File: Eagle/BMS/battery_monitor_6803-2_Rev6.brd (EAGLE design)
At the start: 88.1 x 53.3 mm, 68 parts, among them IC1 MIC2954-03WS, Q1 MOSFET-PCHANNELIRLML2244, Q10 IRF9530, Q2 MOSFET-NCHANNELBSS138, Q3 MOSFET-PCHANNELIRLML2244, Q4 MOSFET-PCHANNELIRLML2244, Q5 MOSFET-PCHANNELIRLML2244, Q6 MOSFET-NCHANNELBSS138, Q7 MOSFET-NCHANNELBSS138, Q8 MOSFET-NCHANNELBSS138, Q9 PMOS_AO4435

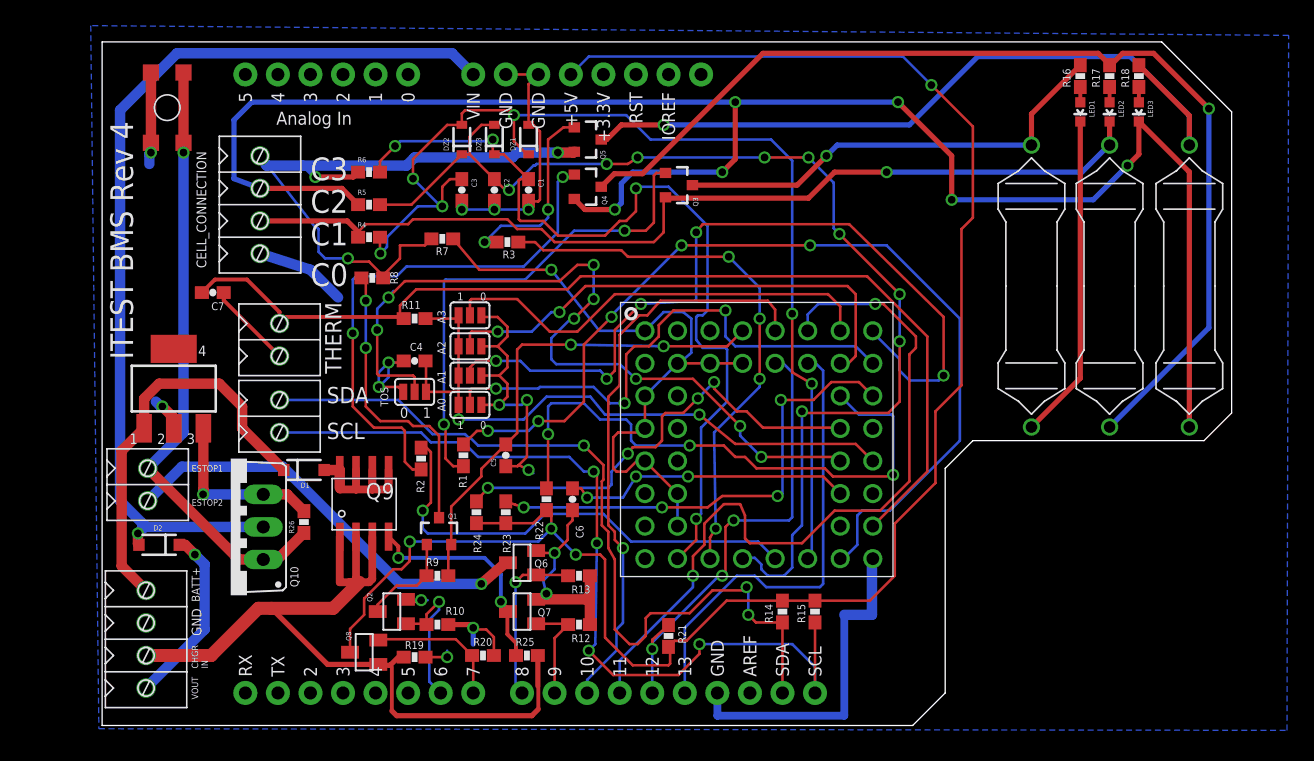
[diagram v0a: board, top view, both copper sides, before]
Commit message: Added voltage regulator to charging circuit of BMS.
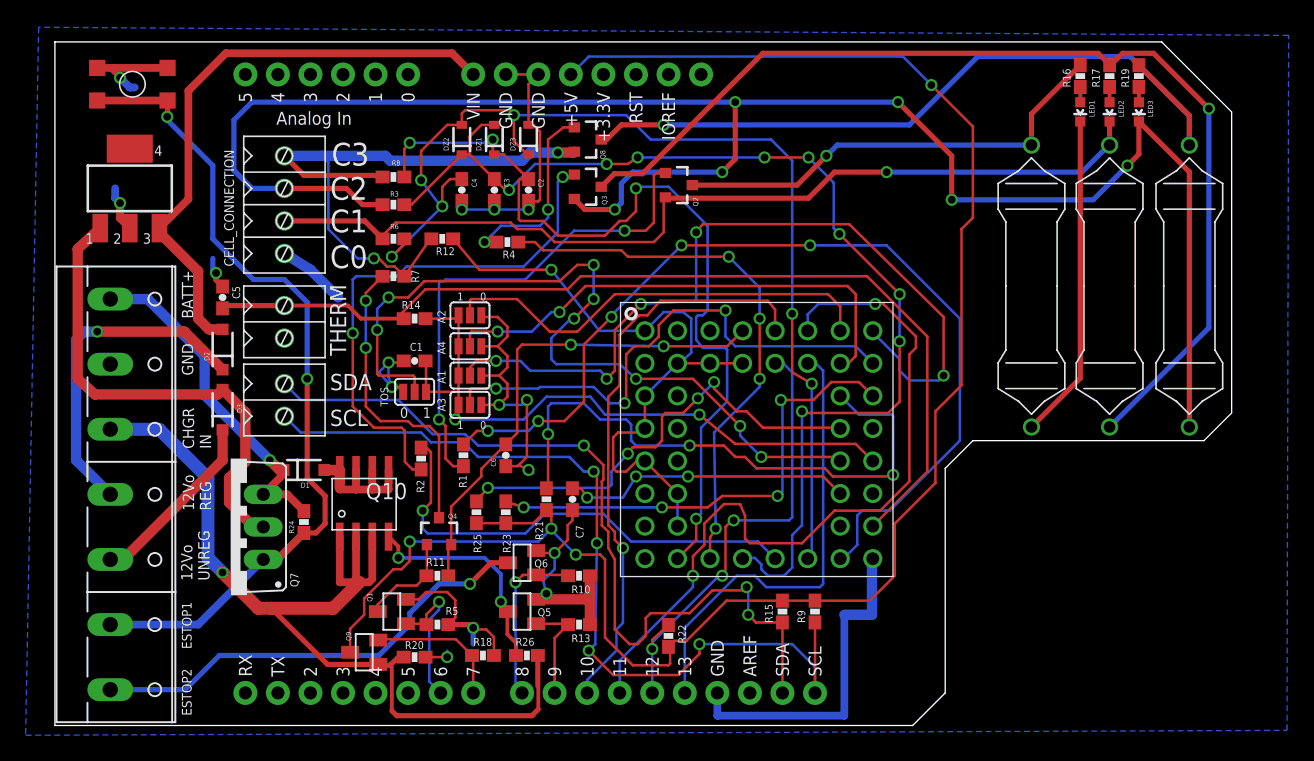
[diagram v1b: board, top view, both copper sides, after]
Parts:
- removed A0: (no value), SparkFun:SJ_3
- removed U$7: TACTILE-SWITCH-7914G, GeekAmmo:7914G
- removed U$8: ARDUINO_R3_SHIELD, SparkFun-Boards:UNO_R3_SHIELD
- removed U$9: LTC6803, Clayton:LTC6803_BREAKOUT
- added A4: (no value), SparkFun:SJ_3
- added D3: SMD26PL-TP, SparkFun-DiscreteSemi:SOD-123
- added U$5: RESISTOR-POWER-3W, isaac1:RESISTOR-3W
- added X1: W237-07P, con-wago-508:W237-7P
- C1: value 0.1uF -> 1uF
- C4: value 1uF -> 0.1uF
- Q1, Q5: value MOSFET-PCHANNELIRLML2244 -> MOSFET-NCHANNELBSS138; device SparkFun-DiscreteSemi:SOT23-3@1 -> SparkFun-DiscreteSemi:SOT23
- Q10: value IRF9530 -> PMOS_AO4435; device Adams Chips:TO220BV -> isaac1:SOIC8
- Q2, Q8: value MOSFET-NCHANNELBSS138 -> MOSFET-PCHANNELIRLML2244; device SparkFun-DiscreteSemi:SOT23 -> SparkFun-DiscreteSemi:SOT23-3@1
- Q7: value MOSFET-NCHANNELBSS138 -> IRF9530; device SparkFun-DiscreteSemi:SOT23 -> Adams Chips:TO220BV
- Q9: value PMOS_AO4435 -> MOSFET-NCHANNELBSS138; device isaac1:SOIC8 -> SparkFun-DiscreteSemi:SOT23
- R11: value 100k -> 4.7k
- R12: value 4.7k -> 100
- R14: value 4.7k -> 100k
- R18: value 470 -> 4.7k
- R19: value 4.7k -> 470
- R21, R25: value 4.7k -> 1Meg
- R22, R26: value 1Meg -> 4.7k
- R3: value 3.3k -> 100
- R4: value 100 -> 3.3k
- R5: value 100 -> 4.7k
- U$2: value RESISTOR-POWER-3W -> TACTILE-SWITCH-7914G; device isaac1:RESISTOR-3W -> GeekAmmo:7914G
- U$4: value SCREW_TERMINAL_4 -> LTC6803; device isaac1:SCREW_TERMINAL_4 -> Clayton:LTC6803_BREAKOUT
- U$6: value SCREW_TERMINAL_2 -> ARDUINO_R3_SHIELD; device Isaac:SCREW_TERMINAL_2 -> SparkFun-Boards:UNO_R3_SHIELD
- moved U$2 80.8 mm to (1.14, 52.1), turned to 270 degrees
- moved R19 72.5 mm to (82.4, 51.4), turned to 90 degrees
- moved R18 68.3 mm to (31.2, 6.22), turned to 180 degrees
- moved U$6 65.0 mm to (67.3, 0.76), turned to 90 degrees
- moved Q8 43.6 mm to (39.4, 46.5), turned to 270 degrees
- moved Q2 40.1 mm to (46.5, 42.9), turned to 270 degrees
- moved U$4 37.3 mm to (41.9, 12.3)
- moved Q5 37.2 mm to (34.3, 9.65), turned to 90 degrees
- moved R14 36.7 mm to (25.9, 32.5), turned to 0 degrees
- moved R5 33.2 mm to (27.7, 8.64), turned to 180 degrees
- moved C7 32.4 mm to (38.2, 18.4), turned to 90 degrees
- moved R12 31.9 mm to (28.1, 38.7), turned to 0 degrees
- moved R9 29.6 mm to (57.1, 9.65), turned to 90 degrees
- moved Q4 29.3 mm to (27.8, 15.9), turned to 0 degrees
- moved C5 25.3 mm to (10.9, 34.2), turned to 270 degrees
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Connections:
- removed net 5VREG: IC1.3, Q10.S, R26.2
- removed net VIN: D2.A, Q10.D, U$8.VIN
- removed net WIRE: D2.C, U$4.P$4
- new net 12VREG: D2.A, IC1.3, U$6.VIN
- new net 12VUNREG: D3.A, IC1.1, Q7.D
- new net N$15: D2.C, X1.4
- new net N$16: D3.C, X1.5
- net +5: now also Q9.3, R21.1, R22.2, R25.1, R9.2, U$6.5V; no longer Q8.3, R14.2, R21.2, R22.1, R24.1, U$8.5V
- net A0: now also A3.2, U$4.AO; no longer A0.2, U$9.AO
- net A1: now also U$4.A1; no longer U$9.A1
- net A2: now also A4.2, U$4.A2; no longer A2.2, U$9.A2
- net A3: now also A2.2, U$4.A3; no longer A3.2, U$9.A3
- net ALL_SYSTEMS_GO: now also R10.2, U$6.D8; no longer R13.2, U$8.D8
- net BATTERY+: now also Q7.S, R24.2, X1.1; no longer IC1.1, U$4.P$1
- net C1: now also C4.1, DZ3.1, R6.2, U$4.C1; no longer C3.1, DZ1.1, R4.2, U$9.C1
- net C12: now also R12.2, U$4.C10, U$4.C11, U$4.C12, U$4.C4, U$4.C5, U$4.C6, U$4.C7, U$4.C8, U$4.C9; no longer R7.2, U$9.C10, U$9.C11, U$9.C12, U$9.C4, U$9.C5, U$9.C6, U$9.C7, U$9.C8, U$9.C9
- net C2: now also C3.1, DZ1.2, R3.2, U$4.C2; no longer C2.1, DZ3.2, R5.2, U$9.C2
- net C3: now also C2.1, DZ1.1, R8.2, U$4.C3; no longer C1.1, DZ3.1, R6.2, U$9.C3
- net CHARGE: now also Q5.1, R13.2, U$6.D9; no longer Q7.1, R12.2, U$8.D9
- net CHARGER_CONNECTED: now also Q9.2, R18.2, U$6.D7; no longer Q8.2, R20.2, U$8.D7
- net CHARGER_IN: now also Q10.1, Q10.2, Q10.3, R20.2, R26.2, X1.3; no longer Q8.1, Q9.2, Q9.3, R19.2, R25.2, U$4.P$3
- net ESTOP1: now also Q7.G, R24.1, U$2.3, U$2.4, X1.6; no longer Q10.G, R26.1, U$6.P$1, U$7.3, U$7.4
- net ESTOP2: now also X1.7; no longer U$6.P$2
- net GND: now also A4.3, DZ3.2, Q1.2, Q5.2, R18.1, R5.1, U$2.1, U$2.2, U$4.V-, U$6.GND@0, U$6.GND@1, U$6.GND@2, X1.2; no longer A0.3, DZ1.2, Q2.2, Q7.2, R12.1, R19.1, U$4.P$2, U$7.1, U$7.2, U$8.GND@0, U$8.GND@1, U$8.GND@2, U$9.V-
- net GPIO1: now also U$4.GPIO1; no longer U$9.GPIO1
- net GPIO2: now also R21.2, U$4.GPIO2; no longer R22.2, U$9.GPIO2
- net MISO: now also R22.1, U$4.SDO, U$6.D12; no longer R21.1, U$8.D12, U$9.SDO
- net MOSI: now also U$4.SDI, U$6.D11; no longer U$8.D11, U$9.SDI
- net N$1: now also Q10.4, Q5.3, R26.1; no longer Q7.3, Q9.4, R25.1
- net N$10: now also Q3.3, U$3.P$1; no longer Q4.3, U$2.P$1
- net N$11: now also Q3.1; no longer Q4.1
- net N$12: now also Q8.3, R19.2, U$5.P$1; no longer Q5.3, R18.2, U$3.P$1
- net N$18: now also Q4.3, R7.2; no longer Q1.3, R8.2
- net N$2: now also Q2.2, R6.1, U$3.P$2; no longer Q3.2, R4.1, U$2.P$2
- net N$20: now also Q1.3, Q4.1, R11.1; no longer Q1.1, Q2.3, R9.1
- net N$23: now also R19.1; no longer R18.1
- net N$29: now also Q8.1, R4.1; no longer Q5.1, R3.1
- net N$3: now also Q3.2, R3.1, U$5.P$2; no longer Q4.2, R5.1, U$3.P$2
- net N$4: now also Q8.2, R12.1; no longer Q5.2, R6.1
- net N$5: now also Q2.3; no longer Q3.3
- net N$7: now also Q2.1; no longer Q3.1
- net N$8: now also Q10.5, Q10.6, Q10.7, Q10.8; no longer Q9.5, Q9.6, Q9.7, Q9.8
- net PWR: now also Q1.1, R5.2, U$6.D6; no longer Q2.1, R10.2, U$8.D6
- net S1: now also U$4.S1; no longer U$9.S1
- net S2: now also U$4.S2; no longer U$9.S2
- net S3: now also R4.2, U$4.S3; no longer R3.2, U$9.S3
- net SCK: now also U$4.SCKI, U$6.D13; no longer U$8.D13, U$9.SCKI
- net SCL: now also R9.1, U$6.SCL; no longer R15.1, U$8.SCL
- net SDA: now also R15.1, U$6.SDA; no longer R14.1, U$8.SDA
- net SS: now also U$4.CSBI, U$6.D10; no longer U$8.D10, U$9.CSBI
- net TOS: now also U$4.TOS; no longer U$9.TOS
- net V+: now also C6.2, Q4.2, R11.2, U$4.V+; no longer C5.2, Q1.2, R9.2, U$9.V+
- net VREF: now also C7.2, U$4.VREF; no longer C6.2, U$9.VREF
- net VREG: now also A4.1, C1.1, R14.2, U$4.VREG; no longer A0.1, C4.1, R11.2, U$9.VREG
- net VTEMP1: now also C5.2, R14.1, U$4.VTEMP1; no longer C7.2, R11.1, U$9.VTEMP1
- net WDTB: now also R25.2, U$4.WDTB; no longer R24.2, U$9.WDTB
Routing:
- net VIN: track 74.4 -> 0.00 mm, vias 1 -> 0
- net 12VREG: track 0.00 -> 46.3 mm
- net 12VUNREG: track 0.00 -> 38.0 mm
- net N$15: track 0.00 -> 26.1 mm, vias 0 -> 1
- net ESTOP1: track 48.0 -> 65.4 mm, vias 1 -> 2
- net N$16: track 0.00 -> 14.3 mm
- net WIRE: track 14.2 -> 0.00 mm, vias 1 -> 0
- net 5VREG: track 13.6 -> 0.00 mm, vias 1 -> 0
- net CHARGER_IN: track 64.2 -> 74.9 mm, vias 0 -> 1
- net BATTERY+: track 31.6 -> 27.1 mm, vias 0 -> 1
- net VTEMP1: track 80.1 -> 76.1 mm
- net N$4: track 52.0 -> 49.5 mm, vias 3 -> 2
- net ESTOP2: track 33.4 -> 35.7 mm
- net N$2: track 74.8 -> 72.8 mm
- net C2: track 88.4 -> 86.5 mm
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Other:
- board size 88.1 x 53.3 mm -> 91.8 x 53.3 mm
- board text added: "12Vo REG"
- board text added: "12Vo UNREG"
- board text added: "ITEST BMS Rev 6"
- board text removed: "ITEST BMS Rev 4"
- board text removed: "VOUT"

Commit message: Changed linear regulator device.
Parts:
- IC1: value MIC2954-03WS -> MIC2920A-12WS
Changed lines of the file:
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@@
 <attribute name="NAME" x="17.018" y="19.304" size="0.4064" layer="25"/>
 </element>
-<element name="IC1" library="linear" package="SOT223" value="MIC2954-03WS" x="3.683" y="42.672" smashed="yes"/>
+<element name="IC1" library="linear" package="SOT223" value="MIC2920A-12WS" x="3.683" y="42.672" smashed="yes"/>
 <element name="X1" library="con-wago-508" package="W237-7P" value="W237-07P" x="2.794" y="18.796" smashed="yes" rot="R270">
 <attribute name="OC_FARNELL" value="unknown" x="2.794" y="18.796" size="1.778" layer="27" rot="R270" display="off"/>
